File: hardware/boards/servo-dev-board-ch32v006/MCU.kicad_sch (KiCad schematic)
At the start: 9 parts, among them J3 PIN-V, SW1 SW_Push, U3 CH32V006F8P6

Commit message: updated LCSC part numbers for all symbols
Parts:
- C11: LCSC C96446 -> C440198
- C12: LCSC C307331 -> C28233
- C13: LCSC C1525 -> C28233
- J3: LCSC (none) -> C65114
- R10: LCSC C11702 -> C17513
- R11: LCSC C25744 -> C17414
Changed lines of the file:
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@@
 			)
 		)
-		(property "LCSC" "C1525"
+		(property "LCSC" "C28233"
 			(at 147.32 58.4199 0)
 			(effects
@@
 			)
 		)
-		(property "LCSC" "C96446"
+		(property "LCSC" "C440198"
 			(at 21.336 53.34 0)
 			(effects
@@
 			)
 		)
+		(property "LCSC" "C65114"
+			(at 67.31 99.06 0)
+			(effects
+				(font
+					(size 1.27 1.27)
+				)
+				(hide yes)
+			)
+		)
 		(pin "4"
 		)
@@
 			)
 		)
-		(property "LCSC" "C25744"
+		(property "LCSC" "C17414"
 			(at 138.43 44.196 0)
 			(effects
@@
 			)
 		)
-		(property "LCSC" "C307331"
+		(property "LCSC" "C28233"
 			(at 32.766 53.34 0)
 			(effects
@@
 			)
 		)
-		(property "LCSC" "C11702"
+		(property "LCSC" "C17513"
 			(at 31.75 101.5999 0)
 			(effects

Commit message: remove 'LCSC Part' Property from project
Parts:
- U3: LCSC Part C52753342 -> (none)
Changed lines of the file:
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@@
-			)
-		)
-		(property "LCSC Part" "C52753342"
-			(at 90.17 82.55 0)
-			(effects
-				(font
-					(size 1.27 1.27)
-				)
-				(hide yes)
 			)
 		)

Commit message: added MFPN properties
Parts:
- C11: MFPN (none) -> GRM21BR61H106KE43L
- C12, C13: MFPN (none) -> CL21B104KCFNNNE
- J3: MFPN (none) -> 2.54-2*3P
- LED3: MFPN (none) -> NCD0805R1
- R10: MFPN (none) -> 0805W8F1001T5E
- R11: MFPN (none) -> 0805W8F1002T5E
- SW1: MFPN (none) -> TS-1088-AR02016
- U3: MFPN (none) -> CH32V006F8P6
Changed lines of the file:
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@@
+			)
+		)
+		(property "MFPN" "CL21B104KCFNNNE"
+			(at 147.32 58.4199 0)
+			(effects
+				(font
+					(size 1.27 1.27)
+				)
+				(hide yes)
 			)
 		)
@@
 			)
 		)
+		(property "MFPN" "NCD0805R1"
+			(at 33.02 112.0774 0)
+			(effects
+				(font
+					(size 1.27 1.27)
+				)
+				(hide yes)
+			)
+		)
 		(property "Sim.Pins" "1=K 2=A"
 			(at 29.21 111.76 0)
@@
 			)
 		)
+		(property "MFPN" "CH32V006F8P6"
+			(at 90.17 82.55 0)
+			(effects
+				(font
+					(size 1.27 1.27)
+				)
+				(hide yes)
+			)
+		)
 		(property "JLC Type" "Extended"
 			(at 91.44 57.15 0)
@@
 		)
 		(property "LCSC" "C720477"
+			(at 161.29 59.69 0)
+			(effects
+				(font
+					(size 1.27 1.27)
+				)
+				(hide yes)
+			)
+		)
+		(property "MFPN" "TS-1088-AR02016"
 			(at 161.29 59.69 0)
 			(effects
@@
 			)
 		)
+		(property "MFPN" "GRM21BR61H106KE43L"
+			(at 21.336 53.34 0)
+			(effects
+				(font
+					(size 1.27 1.27)
+				)
+				(hide yes)
+			)
+		)
 		(pin "1"
 		)
@@
 			)
 		)
+		(property "MFPN" "2.54-2*3P"
+			(at 67.31 99.06 0)
+			(effects
+				(font
+					(size 1.27 1.27)
+				)
+				(hide yes)
+			)
+		)
 		(pin "4"
 		)
@@
 			)
 		)
+		(property "MFPN" "0805W8F1002T5E"
+			(at 138.43 44.196 0)
+			(effects
+				(font
+					(size 1.27 1.27)
+				)
+				(hide yes)
+			)
+		)
 		(pin "1"
 		)
@@
 		)
 		(property "LCSC" "C28233"
+			(at 32.766 53.34 0)
+			(effects
+				(font
+					(size 1.27 1.27)
+				)
+				(hide yes)
+			)
+		)
+		(property "MFPN" "CL21B104KCFNNNE"
 			(at 32.766 53.34 0)
 			(effects
@@
 			(at 31.75 101.5999 0)
 			(effects
+				(font
+					(size 1.27 1.27)
+				)
+				(hide yes)
+			)
+		)
+		(property "MFPN" "0805W8F1001T5E"
+			(at 31.75 101.5999 0)
+			(effects

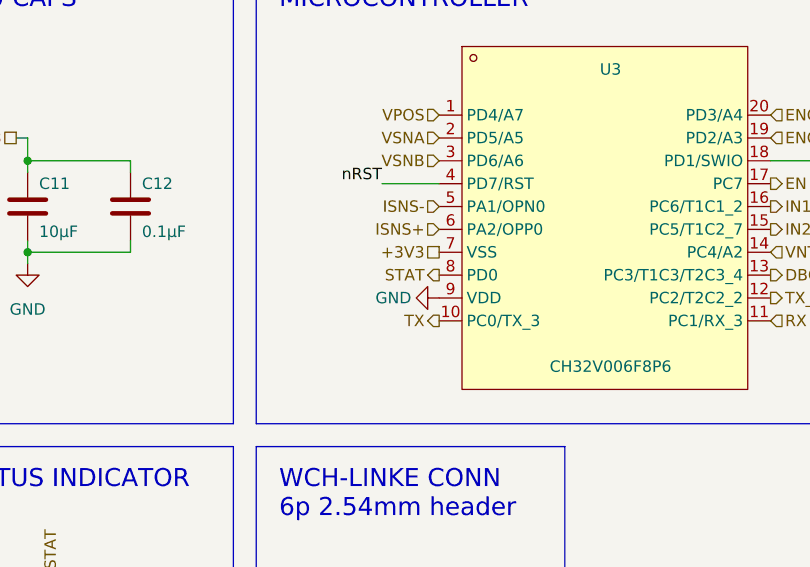
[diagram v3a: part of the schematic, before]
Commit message: Revision V1B. Fixes:
* Fixed reversed VDD/VCC on MCU.
* Fixed TP silk screen labels on top row.
* Updated RS1 to 10mOhm/333mW.
* Updated System (green) LED resistor to 1.5kOhm to reduce brightness.
* Aligned bottom row TPs to center of board.
* Updated text on back silkscreen to reflect version / RS1 updates.
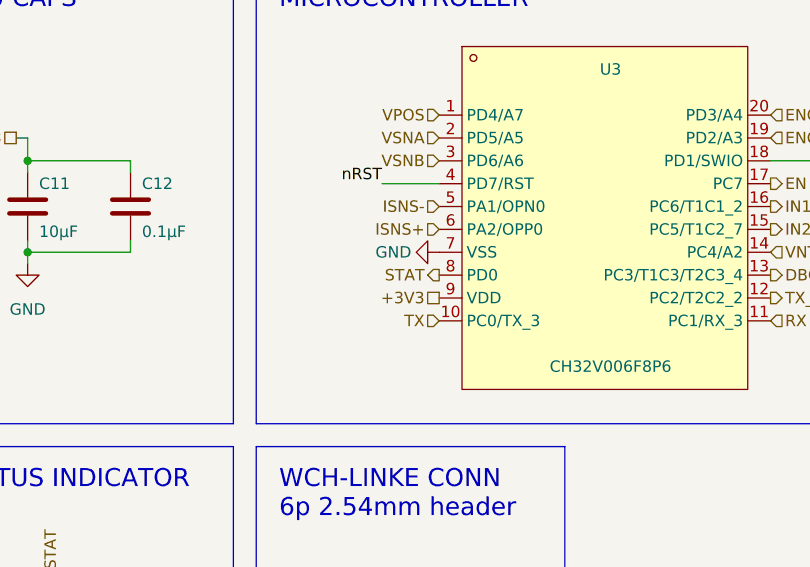
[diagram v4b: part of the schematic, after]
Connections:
- net +3V3: now also U3.9 (VDD); no longer U3.7 (VSS)
- net GND: now also U3.7 (VSS); no longer U3.9 (VDD)

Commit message: update board
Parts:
- removed C13: 0.1µF, Capacitor_SMD:C_0805_2012Metric_Pad1.18x1.45mm_HandSolder, symbol Device:C
- removed R11: 10kΩ, Resistor_SMD:R_0805_2012Metric_Pad1.20x1.40mm_HandSolder, symbol Device:R
- removed SW1: SW_Push, Button_Switch_SMD:SW_SPST_TS-1088-xR020, symbol Switch:SW_Push
- renumbered C12 to C10, C11 to C9, R10 to R12
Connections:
- net DBG: now also U3.8 (PD0); no longer U3.13 (PC3/T1C3/T2C3_4)
- net EN: now also U3.13 (PC3); no longer U3.17 (PC7)
- net ENCB: now also U3.1 (PD4/A7/T2C2_7); no longer U3.19 (PD2/A3)
- net ISNS-: now also U3.4 (PA4/OPN2); no longer U3.5 (PA1/OPN0)
- net STAT: now also U3.17 (T1C4_7/PC7); no longer U3.8 (PD0)
- net VPOS: now also U3.19 (A3/PD2); no longer U3.1 (PD4/A7)
- net nRST renamed VPROG
- net VPROG: no longer U3.4 (PD7/RST)
- new net VSNS: U3.5 (PA1/A1)
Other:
- note removed: "RESET SWITCH"
- moved on the sheet: U3

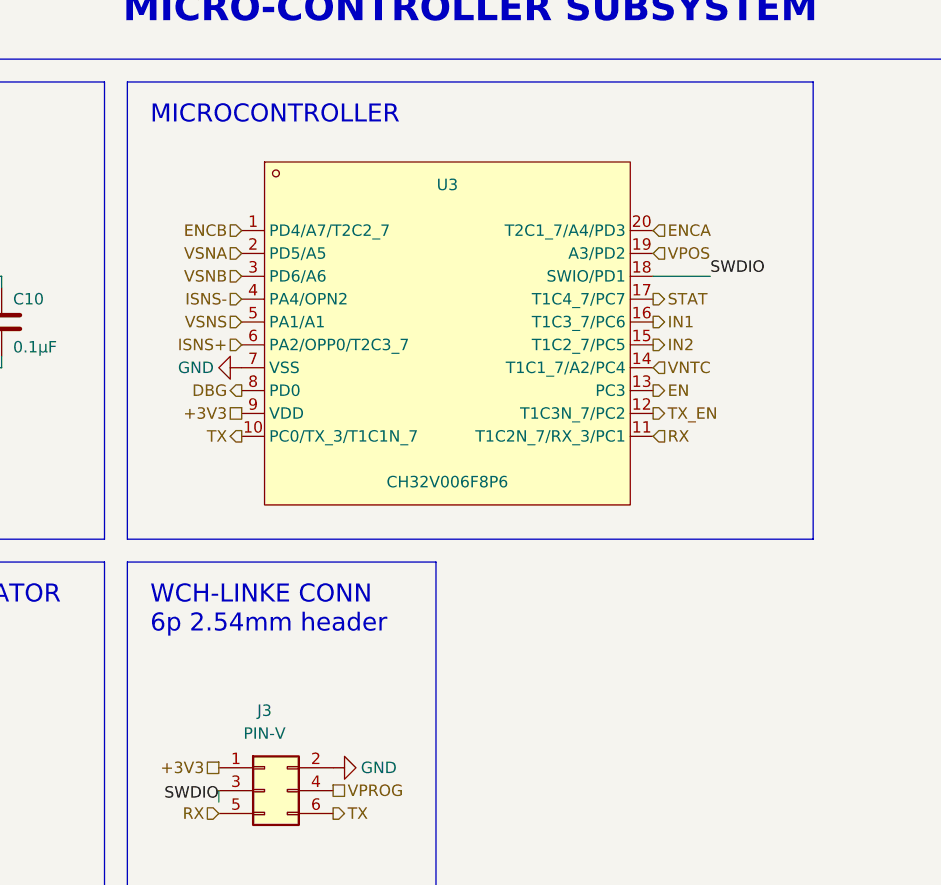
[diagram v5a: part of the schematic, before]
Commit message: updated schematics. ERC on schematics is now passing
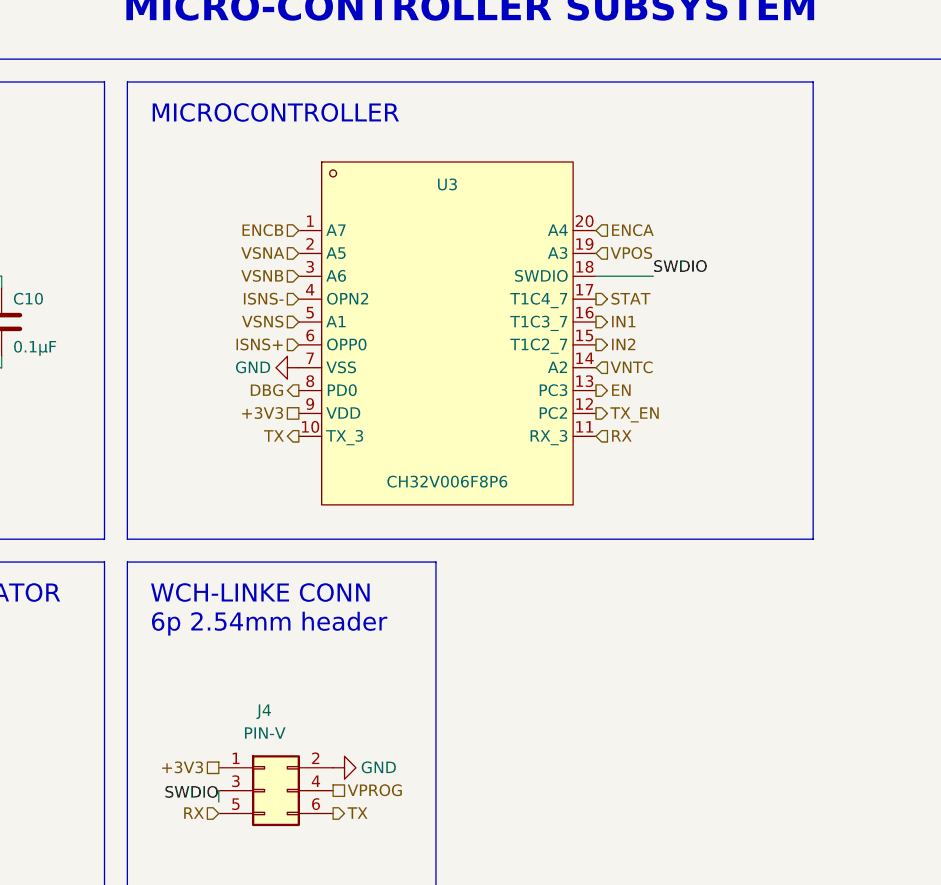
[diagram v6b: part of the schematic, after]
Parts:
- renumbered J3 to J4
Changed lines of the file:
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@@
 	(wire
 		(pts
-			(xy 116.84 50.8) (xy 110.49 50.8)
+			(xy 110.49 50.8) (xy 104.14 50.8)
 		)
 		(stroke
@@
 	)
 	(label "SWDIO"
-		(at 116.84 50.8 0)
+		(at 110.49 50.8 0)
 		(effects
 			(font
@@
 	(hierarchical_label "IN1"
 		(shape output)
-		(at 110.49 55.88 0)
+		(at 104.14 55.88 0)
 		(effects
 			(font
@@
 	(hierarchical_label "VSNS"
 		(shape input)
-		(at 64.77 55.88 180)
+		(at 71.12 55.88 180)
 		(effects
 			(font
@@
 	(hierarchical_label "ENCA"
 		(shape input)
-		(at 110.49 45.72 0)
+		(at 104.14 45.72 0)
 		(effects
 			(font
@@
 	(hierarchical_label "ISNS-"
 		(shape input)
-		(at 64.77 53.34 180)
+		(at 71.12 53.34 180)
 		(effects
 			(font
@@
 	(hierarchical_label "EN"
 		(shape output)
-		(at 110.49 63.5 0)
+		(at 104.14 63.5 0)
 		(effects
 			(font
@@
 	(hierarchical_label "VSNB"
 		(shape input)
-		(at 64.77 50.8 180)
+		(at 71.12 50.8 180)
 		(effects
 			(font
@@
 	(hierarchical_label "RX"
 		(shape input)
-		(at 110.49 68.58 0)
+		(at 104.14 68.58 0)
 		(effects
 			(font
@@
 	(hierarchical_label "ENCB"
 		(shape input)
-		(at 64.77 45.72 180)
+		(at 71.12 45.72 180)
 		(effects
 			(font
@@
 	(hierarchical_label "STAT"
 		(shape output)
-		(at 110.49 53.34 0)
+		(at 104.14 53.34 0)
 		(effects
 			(font
@@
 	(hierarchical_label "IN2"
 		(shape output)
-		(at 110.49 58.42 0)
+		(at 104.14 58.42 0)
 		(effects
 			(font
@@
 	(hierarchical_label "ISNS+"
 		(shape input)
-		(at 64.77 58.42 180)
+		(at 71.12 58.42 180)
 		(effects
 			(font
@@
 	(hierarchical_label "VSNA"
 		(shape input)
-		(at 64.77 48.26 180)
+		(at 71.12 48.26 180)
 		(effects
 			(font
@@
 	(hierarchical_label "TX"
 		(shape output)
-		(at 64.77 68.58 180)
+		(at 71.12 68.58 180)
 		(effects
 			(font
@@
 	(hierarchical_label "+3V3"
 		(shape passive)
-		(at 64.77 66.04 180)
+		(at 71.12 66.04 180)
 		(effects
 			(font
@@
 	(hierarchical_label "TX_EN"
 		(shape output)
-		(at 110.49 66.04 0)
+		(at 104.14 66.04 0)
 		(effects
 			(font
@@
 	(hierarchical_label "VPOS"
 		(shape input)
-		(at 110.49 48.26 0)
+		(at 104.14 48.26 0)
 		(effects
 			(font
@@
 	(hierarchical_label "VNTC"
 		(shape input)
-		(at 110.49 60.96 0)
+		(at 104.14 60.96 0)
 		(effects
 			(font
@@
 	(hierarchical_label "DBG"
 		(shape output)
-		(at 64.77 63.5 180)
+		(at 71.12 63.5 180)
 		(effects
 			(font
@@
 		(in_pos_files yes)
 		(dnp no)
-		(property "Reference" "#PWR033"
+		(property "Reference" "#PWR039"
 			(at 26.67 68.58 0)
 			(hide yes)
@@
 			(project "servo-dev-board-ch32v006"
 				(path "/6062e7d2-0c72-467e-b49c-6387ba053e09/77d3819f-1672-490a-859c-8df54ad0ab77"
-					(reference "#PWR033")
+					(reference "#PWR039")
 					(unit 1)
 				)
@@
 		)
 		(pin "5"
+			(alternate "A1")
 		)
 		(pin "9"
@@
 		)
 		(pin "3"
+			(alternate "A6")
 		)
 		(pin "6"
+			(alternate "OPP0")
 		)
 		(pin "2"
+			(alternate "A5")
 		)
 		(pin "4"
+			(alternate "OPN2")
 		)
 		(pin "1"
+			(alternate "A7")
 		)
 		(pin "11"
+			(alternate "RX_3")
 		)
 		(pin "15"
+			(alternate "T1C2_7")
 		)
 		(pin "12"
@@
 		)
 		(pin "14"
+			(alternate "A2")
 		)
 		(pin "18"
+			(alternate "SWDIO")
 		)
 		(pin "19"
+			(alternate "A3")
 		)
 		(pin "10"
+			(alternate "TX_3")
 		)
 		(pin "20"
+			(alternate "A4")
 		)
 		(pin "17"
+			(alternate "T1C4_7")
 		)
 		(pin "16"
+			(alternate "T1C3_7")
 		)
 		(instances
@@
 		(dnp no)
 		(fields_autoplaced yes)
-		(property "Reference" "#PWR034"
+		(property "Reference" "#PWR040"
 			(at 29.21 124.46 0)
 			(hide yes)
@@
 			(project "servo-dev-board-ch32v006"
 				(path "/6062e7d2-0c72-467e-b49c-6387ba053e09/77d3819f-1672-490a-859c-8df54ad0ab77"
-					(reference "#PWR034")
+					(reference "#PWR040")
 					(unit 1)
 				)
@@
 	(symbol
 		(lib_id "power:GND")
-		(at 64.77 60.96 270)
+		(at 71.12 60.96 270)
 		(unit 1)
 		(body_style 1)
@@
 		(in_pos_files yes)
 		(dnp no)
-		(property "Reference" "#PWR035"
-			(at 58.42 60.96 0)
+		(property "Reference" "#PWR041"
+			(at 64.77 60.96 0)
 			(hide yes)
 			(show_name no)
@@
 		)
 		(property "Value" "GND"
-			(at 59.69 60.96 90)
+			(at 66.04 60.96 90)
 			(show_name no)
 			(do_not_autoplace no)
@@
 		)
 		(property "Footprint" ""
-			(at 64.77 60.96 0)
+			(at 71.12 60.96 0)
 			(hide yes)
 			(show_name no)
@@
 		)
 		(property "Datasheet" ""
-			(at 64.77 60.96 0)
+			(at 71.12 60.96 0)
 			(hide yes)
 			(show_name no)
@@
 		)
 		(property "Description" "Power symbol creates a global label with name \"GND\" , ground"
-			(at 64.77 60.96 0)
+			(at 71.12 60.96 0)
 			(hide yes)
 			(show_name no)
@@
 			(project "servo-dev-board-ch32v006"
 				(path "/6062e7d2-0c72-467e-b49c-6387ba053e09/77d3819f-1672-490a-859c-8df54ad0ab77"
-					(reference "#PWR035")
+					(reference "#PWR041")
 					(unit 1)
 				)
@@
 		(in_pos_files yes)
 		(dnp no)
-		(property "Reference" "J3"
+		(property "Reference" "J4"
 			(at 67.31 99.06 0)
 			(show_name no)
@@
 			(project "servo-dev-board-ch32v006"
 				(path "/6062e7d2-0c72-467e-b49c-6387ba053e09/77d3819f-1672-490a-859c-8df54ad0ab77"
-					(reference "J3")
+					(reference "J4")
 					(unit 1)
 				)
@@
 		(in_pos_files yes)
 		(dnp no)
-		(property "Reference" "#PWR036"
+		(property "Reference" "#PWR042"
 			(at 81.28 105.41 0)
 			(hide yes)
@@
 			(project "servo-dev-board-ch32v006"
 				(path "/6062e7d2-0c72-467e-b49c-6387ba053e09/77d3819f-1672-490a-859c-8df54ad0ab77"
-					(reference "#PWR036")
+					(reference "#PWR042")
 					(unit 1)
 				)

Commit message: completed routing.
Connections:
- net +3V3: now also J4.3 (Pin_3); no longer J4.1 (Pin_1)
- net DBG: now also U3.13 (PC3); no longer U3.8 (PD0)
- net EN: now also U3.8 (PD0); no longer U3.13 (PC3)
- net ENCA: now also U3.1 (PD4); no longer U3.20 (PD3)
- net ENCB: now also U3.20 (PD3); no longer U3.1 (PD4)
- net GND: now also J4.4 (Pin_4); no longer J4.2 (Pin_2)
- net RX: now also J4.1 (Pin_1); no longer J4.5 (Pin_5)
- net SWDIO: now also J4.5 (Pin_5); no longer J4.3 (Pin_3)
- net TX: now also J4.2 (Pin_2); no longer J4.6 (Pin_6)
- net VPROG: now also J4.6 (Pin_6); no longer J4.4 (Pin_4)
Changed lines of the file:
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@@
+	(wire
+		(pts
+			(xy 62.23 111.76) (xy 62.23 110.49)
+		)
+		(stroke
+			(width 0)
+			(type default)
+		)
+	)
 	(wire
 		(pts
@@
 	(wire
 		(pts
-			(xy 62.23 109.22) (xy 62.23 107.95)
+			(xy 29.21 106.68) (xy 29.21 107.95)
 		)
 		(stroke
@@
 	(wire
 		(pts
-			(xy 29.21 106.68) (xy 29.21 107.95)
+			(xy 26.67 48.26) (xy 26.67 50.8)
 		)
 		(stroke
@@
 	(wire
 		(pts
-			(xy 26.67 48.26) (xy 26.67 50.8)
+			(xy 26.67 59.69) (xy 26.67 60.96)
 		)
 		(stroke
@@
 	(wire
 		(pts
-			(xy 26.67 59.69) (xy 26.67 60.96)
+			(xy 26.67 50.8) (xy 38.1 50.8)
 		)
 		(stroke
@@
 	(wire
 		(pts
-			(xy 26.67 50.8) (xy 38.1 50.8)
+			(xy 26.67 52.07) (xy 26.67 50.8)
 		)
 		(stroke
@@
 	(wire
 		(pts
-			(xy 26.67 52.07) (xy 26.67 50.8)
+			(xy 38.1 50.8) (xy 38.1 52.07)
 		)
 		(stroke
@@
 	(wire
 		(pts
-			(xy 38.1 50.8) (xy 38.1 52.07)
+			(xy 38.1 60.96) (xy 38.1 59.69)
 		)
 		(stroke
@@
 	(wire
 		(pts
-			(xy 38.1 60.96) (xy 38.1 59.69)
+			(xy 29.21 97.79) (xy 29.21 99.06)
 		)
 		(stroke
@@
 		)
 	)
-	(wire
-		(pts
-			(xy 29.21 97.79) (xy 29.21 99.06)
-		)
-		(stroke
-			(width 0)
-			(type default)
-		)
-	)
 	(label "SWDIO"
-		(at 62.23 109.22 180)
+		(at 62.23 111.76 180)
 		(effects
 			(font
@@
 		)
 	)
-	(hierarchical_label "ENCA"
-		(shape input)
-		(at 104.14 45.72 0)
-		(effects
-			(font
-				(size 1.27 1.27)
-			)
-			(justify left)
-		)
-	)
 	(hierarchical_label "ISNS-"
 		(shape input)
@@
 		)
 	)
-	(hierarchical_label "EN"
-		(shape output)
-		(at 104.14 63.5 0)
-		(effects
-			(font
-				(size 1.27 1.27)
-			)
-			(justify left)
+	(hierarchical_label "ENCA"
+		(shape input)
+		(at 71.12 45.72 180)
+		(effects
+			(font
+				(size 1.27 1.27)
+			)
+			(justify right)
 		)
 	)
@@
 	(hierarchical_label "VPROG"
 		(shape passive)
-		(at 74.93 107.95 0)
+		(at 74.93 110.49 0)
 		(effects
 			(font
@@
 		)
 	)
-	(hierarchical_label "ENCB"
-		(shape input)
-		(at 71.12 45.72 180)
-		(effects
-			(font
-				(size 1.27 1.27)
-			)
-			(justify right)
-		)
-	)
 	(hierarchical_label "STAT"
 		(shape output)
@@
 		)
 	)
-	(hierarchical_label "TX"
+	(hierarchical_label "EN"
 		(shape output)
-		(at 74.93 110.49 0)
-		(effects
-			(font
-				(size 1.27 1.27)
-			)
-			(justify left)
+		(at 71.12 63.5 180)
+		(effects
+			(font
+				(size 1.27 1.27)
+			)
+			(justify right)
 		)
 	)
@@
 		)
 	)
-	(hierarchical_label "RX"
-		(shape input)
-		(at 62.23 110.49 180)
+	(hierarchical_label "+3V3"
+		(shape passive)
+		(at 62.23 107.95 180)
 		(effects
 			(font
@@
 		)
 	)
+	(hierarchical_label "RX"
+		(shape input)
+		(at 62.23 105.41 180)
+		(effects
+			(font
+				(size 1.27 1.27)
+			)
+			(justify right)
+		)
+	)
 	(hierarchical_label "+3V3"
 		(shape passive)
@@
 		)
 	)
+	(hierarchical_label "TX"
+		(shape output)
+		(at 74.93 105.41 0)
+		(effects
+			(font
+				(size 1.27 1.27)
+			)
+			(justify left)
+		)
+	)
 	(hierarchical_label "+3V3"
 		(shape passive)
@@
 		)
 	)
+	(hierarchical_label "DBG"
+		(shape output)
+		(at 104.14 63.5 0)
+		(effects
+			(font
+				(size 1.27 1.27)
+			)
+			(justify left)
+		)
+	)
 	(hierarchical_label "TX_EN"
 		(shape output)
@@
 		)
 	)
-	(hierarchical_label "+3V3"
-		(shape passive)
-		(at 62.23 105.41 180)
-		(effects
-			(font
-				(size 1.27 1.27)
-			)
-			(justify right)
-		)
-	)
 	(hierarchical_label "VPOS"
 		(shape input)
@@
 		)
 	)
+	(hierarchical_label "ENCB"
+		(shape input)
+		(at 104.14 45.72 0)
+		(effects
+			(font
+				(size 1.27 1.27)
+			)
+			(justify left)
+		)
+	)
 	(hierarchical_label "VNTC"
 		(shape input)
@@
 			)
 			(justify left)
-		)
-	)
-	(hierarchical_label "DBG"
-		(shape output)
-		(at 71.12 63.5 180)
-		(effects
-			(font
-				(size 1.27 1.27)
-			)
-			(justify right)
 		)
 	)
@@
 	)
 	(symbol
+		(lib_id "power:GND")
+		(at 74.93 107.95 90)
+		(unit 1)
+		(body_style 1)
+		(exclude_from_sim no)
+		(in_bom yes)
+		(on_board yes)
+		(in_pos_files yes)
+		(dnp no)
+		(property "Reference" "#PWR042"
+			(at 81.28 107.95 0)
+			(hide yes)
+			(show_name no)
+			(do_not_autoplace no)
+			(effects
+				(font
+					(size 1.27 1.27)
+				)
+			)
+		)
+		(property "Value" "GND"
+			(at 80.01 107.95 90)
+			(show_name no)
+			(do_not_autoplace no)
+			(effects
+				(font
+					(size 1.27 1.27)
+				)
+			)
+		)
+		(property "Footprint" ""
+			(at 74.93 107.95 0)
+			(hide yes)
+			(show_name no)
+			(do_not_autoplace no)
+			(effects
+				(font
+					(size 1.27 1.27)
+				)
+			)
+		)
+		(property "Datasheet" ""
+			(at 74.93 107.95 0)
+			(hide yes)
+			(show_name no)
+			(do_not_autoplace no)
+			(effects
+				(font
+					(size 1.27 1.27)
+				)
+			)
+		)
+		(property "Description" "Power symbol creates a global label with name \"GND\" , ground"
+			(at 74.93 107.95 0)
+			(hide yes)
+			(show_name no)
+			(do_not_autoplace no)
+			(effects
+				(font
+					(size 1.27 1.27)
+				)
+			)
+		)
+		(pin "1"
+		)
+		(instances
+			(project "servo-dev-board-ch32v006"
+				(path "/6062e7d2-0c72-467e-b49c-6387ba053e09/77d3819f-1672-490a-859c-8df54ad0ab77"
+					(reference "#PWR042")
+					(unit 1)
+				)
+			)
+		)
+	)
+	(symbol
 		(lib_id "Device:R")
 		(at 29.21 102.87 0)
@@
 					(unit 1)
 				)
-			)
-		)
-	)
-	(symbol
-		(lib_id "power:GND")
-		(at 74.93 105.41 90)
-		(unit 1)
-		(body_style 1)
-		(exclude_from_sim no)
-		(in_bom yes)
-		(on_board yes)
-		(in_pos_files yes)
-		(dnp no)
-		(property "Reference" "#PWR042"
-			(at 81.28 105.41 0)
-			(hide yes)
-			(show_name no)
-			(do_not_autoplace no)
-			(effects
-				(font
-					(size 1.27 1.27)
-				)
-			)
-		)
-		(property "Value" "GND"
-			(at 80.01 105.41 90)
-			(show_name no)
-			(do_not_autoplace no)
-			(effects
-				(font
-					(size 1.27 1.27)
-				)
-			)
-		)
-		(property "Footprint" ""
-			(at 74.93 105.41 0)
-			(hide yes)
-			(show_name no)
-			(do_not_autoplace no)
-			(effects
-				(font
-					(size 1.27 1.27)
-				)
-			)
-		)
-		(property "Datasheet" ""
-			(at 74.93 105.41 0)
-			(hide yes)
-			(show_name no)
-			(do_not_autoplace no)
-			(effects
-				(font
-					(size 1.27 1.27)
-				)
-			)
-		)
-		(property "Description" "Power symbol creates a global label with name \"GND\" , ground"
-			(at 74.93 105.41 0)
-			(hide yes)
-			(show_name no)
-			(do_not_autoplace no)
-			(effects
-				(font
-					(size 1.27 1.27)
-				)
-			)
-		)
-		(pin "1"
-		)
-		(instances
-			(project "servo-dev-board-ch32v006"
-				(path "/6062e7d2-0c72-467e-b49c-6387ba053e09/77d3819f-1672-490a-859c-8df54ad0ab77"
-					(reference "#PWR042")
-					(unit 1)
-				)
